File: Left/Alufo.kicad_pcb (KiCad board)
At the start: 2 copper layers, 139.7 x 88.9 mm, 67 parts, among them J1 USB_C_Receptacle_USB2.0_16P_2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, J3 USB_C_Receptacle_USB2.0_16P_2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, K11 PG1350, K12 PG1350, K13 PG1350, K14 PG1350, K15 PG1350, K16 PG1350, K21 PG1350, K22 PG1350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

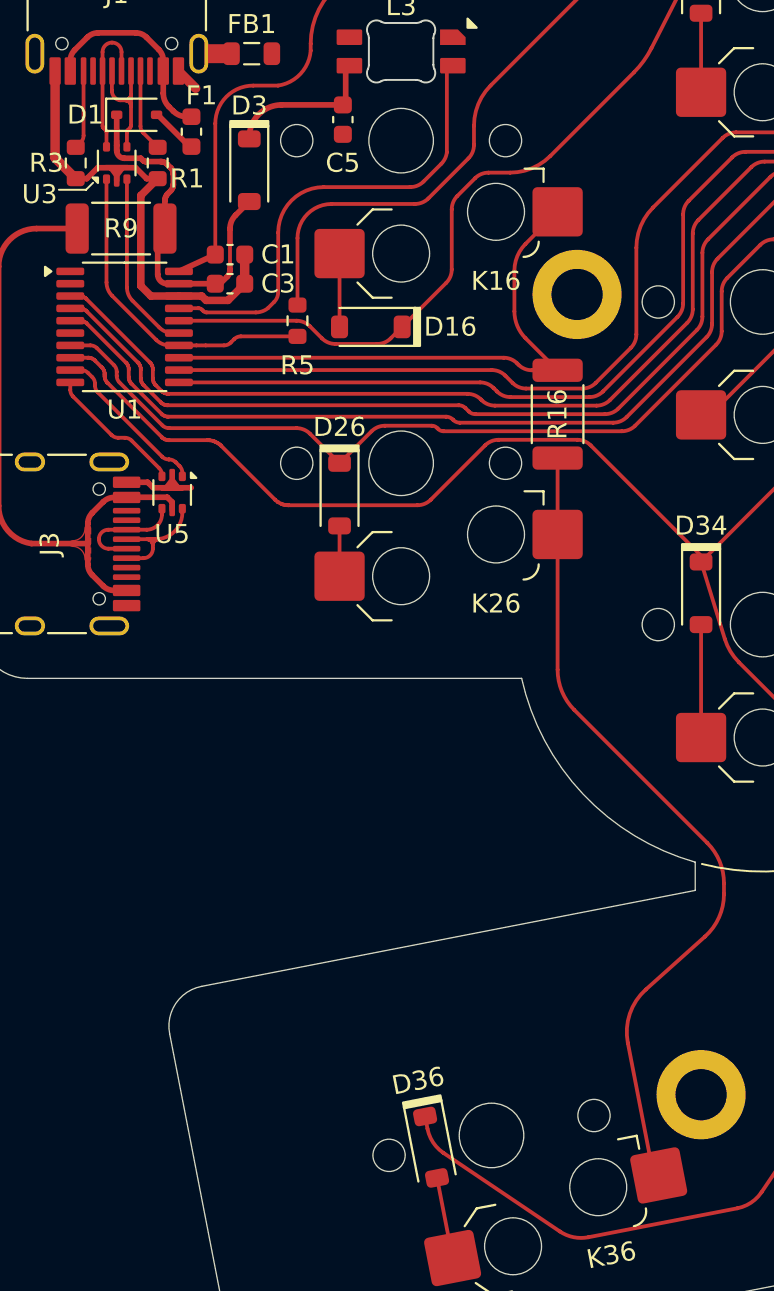
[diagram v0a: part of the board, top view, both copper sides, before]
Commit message: Power routing tweaks
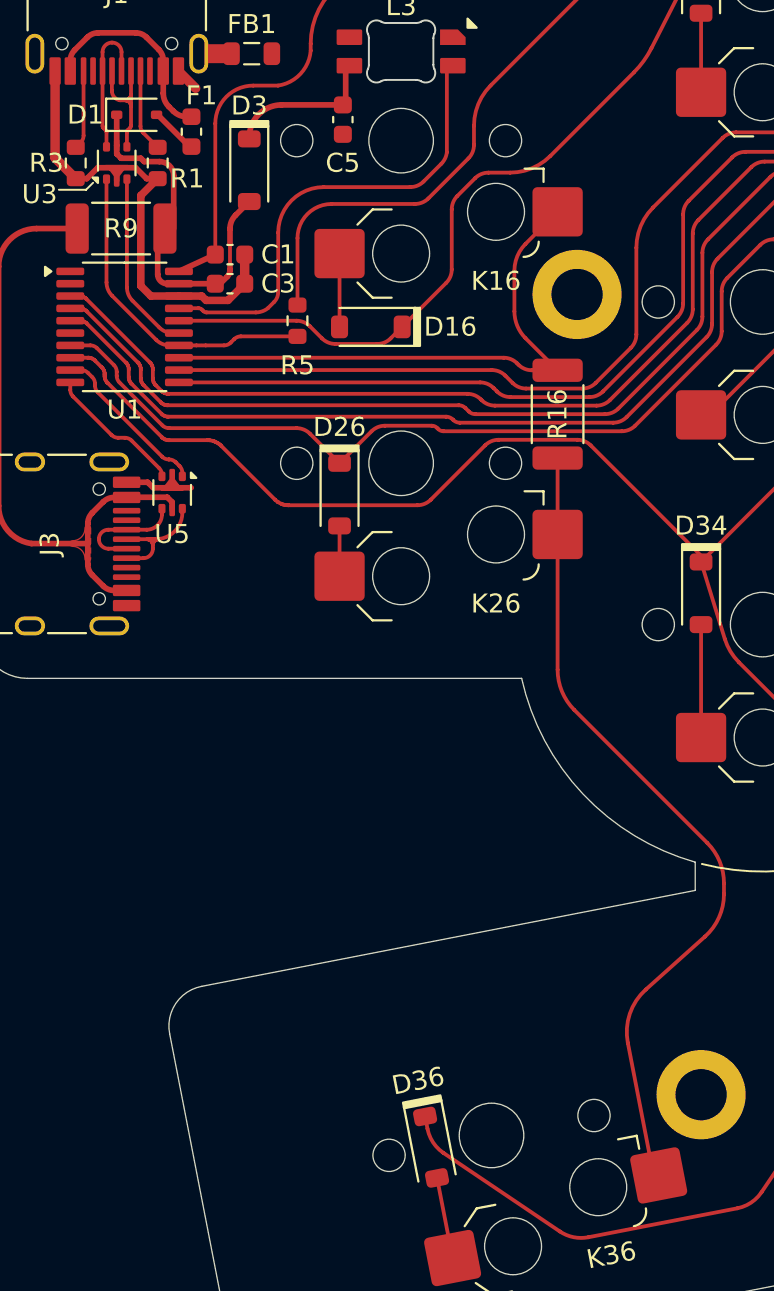
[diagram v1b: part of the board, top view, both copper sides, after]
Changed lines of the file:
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@@
 		(fp_arc
 			(start 1.749484 0.919719)
-			(mid 1.712511 0.81407)
+			(mid 1.712517 0.81407)
 			(end 1.699999 0.702842)
 			(stroke
@@
 		(fp_arc
 			(start 1.699999 -0.702843)
-			(mid 1.712528 -0.814069)
+			(mid 1.712527 -0.814069)
 			(end 1.749484 -0.919721)
 			(stroke
@@
 		(fp_arc
 			(start -1.749484 -0.919721)
-			(mid -1.638071 -1.504035)
+			(mid -1.638071 -1.504036)
 			(end -1.046711 -1.568299)
 			(stroke
@@
 		(net 47)
 	)
-	(segment
-		(start 118.038342 106.733149)
-		(end 118.34685 106.94124)
-		(width 0.2)
-		(layer "F.Cu")
-		(net 47)
-	)
 	(arc
 		(start 121.786884 92.118427)
@@
 	)
 	(segment
-		(start 91.277386 53.517356)
-		(end 91.316843 53.519)
-		(width 0.3)
-		(layer "F.Cu")
-		(net 61)
-	)
-	(segment
-		(start 92.737128 54.000498)
-		(end 92.771059 54.127177)
-		(width 0.3)
-		(layer "F.Cu")
-		(net 61)
-	)
-	(segment
-		(start 92.771059 54.127177)
-		(end 92.773 54.192749)
-		(width 0.3)
-		(layer "F.Cu")
-		(net 61)
-	)
-	(segment
-		(start 92.405061 53.620464)
-		(end 92.452805 53.665447)
-		(width 0.3)
-		(layer "F.Cu")
-		(net 61)
-	)
-	(segment
-		(start 92.164819 53.520976)
-		(end 92.291489 53.554905)
-		(width 0.3)
-		(layer "F.Cu")
-		(net 61)
-	)
-	(segment
 		(start 95.758 58.9915)
 		(end 95.758 57.8485)
@@
 	)
 	(segment
-		(start 92.099251 53.519)
-		(end 92.164819 53.520976)
-		(width 0.3)
-		(layer "F.Cu")
-		(net 61)
-	)
-	(segment
 		(start 89.789 51.054)
 		(end 89.789 52.669)
@@
 	)
 	(segment
-		(start 92.773 54.192749)
-		(end 92.773 54.713225)
-		(width 0.3)
-		(layer "F.Cu")
-		(net 61)
-	)
-	(segment
-		(start 92.291489 53.554905)
-		(end 92.405061 53.620464)
-		(width 0.3)
-		(layer "F.Cu")
-		(net 61)
-	)
-	(segment
 		(start 93.067 59.955)
 		(end 92.448 59.955)
@@
 	)
 	(segment
-		(start 92.626554 53.839196)
-		(end 92.671564 53.886918)
-		(width 0.3)
-		(layer "F.Cu")
-		(net 61)
-	)
-	(segment
-		(start 91.175422 53.460422)
-		(end 91.204473 53.487171)
-		(width 0.3)
-		(layer "F.Cu")
-		(net 61)
-	)
-	(segment
-		(start 92.331442 55.505367)
-		(end 92.3295 55.570939)
-		(width 0.3)
-		(layer "F.Cu")
-		(net 61)
-	)
-	(segment
-		(start 89.789 52.669)
-		(end 89.789 52.944001)
-		(width 0.3)
-		(layer "F.Cu")
-		(net 61)
-	)
-	(segment
-		(start 92.475946 55.217386)
-		(end 92.43094 55.265112)
-		(width 0.3)
-		(layer "F.Cu")
-		(net 61)
-	)
-	(segment
-		(start 91.059001 53.344001)
-		(end 91.175422 53.460422)
-		(width 0.3)
-		(layer "F.Cu")
-		(net 61)
-	)
-	(segment
-		(start 92.452805 53.665447)
-		(end 92.626554 53.839196)
+		(start 95.758 57.055214)
+		(end 95.758 57.8485)
 		(width 0.3)
 		(layer "F.Cu")
@@
 	)
 	(segment
-		(start 95.758 57.055214)
-		(end 95.758 57.8485)
+		(start 91.235976 53.520976)
+		(end 91.059001 53.344001)
 		(width 0.3)
 		(layer "F.Cu")
@@
 	)
 	(segment
-		(start 91.204473 53.487171)
-		(end 91.277386 53.517356)
-		(width 0.3)
-		(layer "F.Cu")
-		(net 61)
-	)
-	(segment
-		(start 92.736941 54.905394)
-		(end 92.671391 55.018921)
-		(width 0.3)
-		(layer "F.Cu")
-		(net 61)
-	)
-	(segment
-		(start 91.316843 53.519)
-		(end 92.099251 53.519)
+		(start 91.059001 53.344001)
+		(end 90.01979 53.344001)
 		(width 0.3)
 		(layer "F.Cu")
@@
 	)
 	(segment
-		(start 92.365376 55.37869)
-		(end 92.331442 55.505367)
-		(width 0.3)
-		(layer "F.Cu")
-		(net 61)
-	)
-	(segment
-		(start 92.43094 55.265112)
-		(end 92.365376 55.37869)
+		(start 90.01979 53.344001)
+		(end 89.789 53.113211)
 		(width 0.3)
 		(layer "F.Cu")
@@
 	)
 	(segment
-		(start 92.770876 54.778771)
-		(end 92.736941 54.905394)
-		(width 0.3)
-		(layer "F.Cu")
-		(net 61)
-	)
-	(segment
-		(start 92.3295 55.570939)
-		(end 92.3295 56.642)
+		(start 92.791999 57.0484)
+		(end 92.791999 54.270976)
 		(width 0.3)
 		(layer "F.Cu")
@@
 	)
 	(segment
-		(start 92.626553 55.066779)
-		(end 92.475946 55.217386)
+		(start 92.041999 53.520976)
+		(end 91.235976 53.520976)
 		(width 0.3)
 		(layer "F.Cu")
@@
 	)
 	(segment
-		(start 90.189 53.344001)
-		(end 91.059001 53.344001)
-		(width 0.3)
-		(layer "F.Cu")
-		(net 61)
-	)
-	(segment
-		(start 92.671391 55.018921)
-		(end 92.626553 55.066779)
-		(width 0.3)
-		(layer "F.Cu")
-		(net 61)
-	)
-	(segment
-		(start 92.773 54.713225)
-		(end 92.770876 54.778771)
-		(width 0.3)
-		(layer "F.Cu")
-		(net 61)
-	)
-	(segment
-		(start 92.671564 53.886918)
-		(end 92.737128 54.000498)
+		(start 89.789 53.113211)
+		(end 89.789 52.669)
 		(width 0.3)
 		(layer "F.Cu")
@@
 	)
 	(arc
-		(start 89.789 52.944001)
-		(mid 89.906157 53.226844)
-		(end 90.189 53.344001)
+		(start 95.758 59.228893)
+		(mid 95.71994 59.420234)
+		(end 95.611554 59.582446)
 		(width 0.3)
 		(layer "F.Cu")
@@
 	)
 	(arc
-		(start 95.758 59.228893)
-		(mid 95.71994 59.420234)
-		(end 95.611554 59.582446)
+		(start 92.791999 54.270976)
+		(mid 92.572329 53.740646)
+		(end 92.041999 53.520976)
 		(width 0.3)
 		(layer "F.Cu")
@@
 		(width 0.3)
 		(layer "F.Cu")
-		(net 62)
-	)
-	(segment
-		(start 93.479714 51.1555)
-		(end 93.726 51.1555)
-		(width 0.3)
-		(layer "F.Cu")

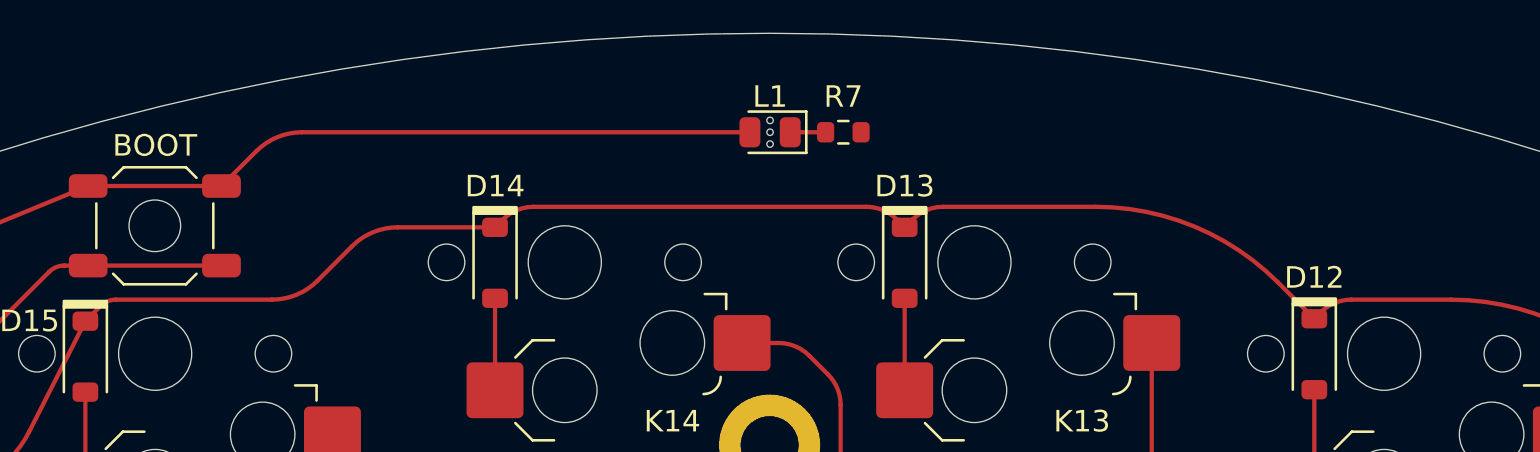
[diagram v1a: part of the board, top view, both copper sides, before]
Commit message: Fix boot access hole location
Because the lefthand side PCB will become the base for the righthand board (and vice versa), and because the boot button is no longer centred, the hole in the base to allow access to the button must be on the opposite side of the centreline to that button. This means the access hole needs to be a separate component and the boot switch footprint no longer needs a central hole.
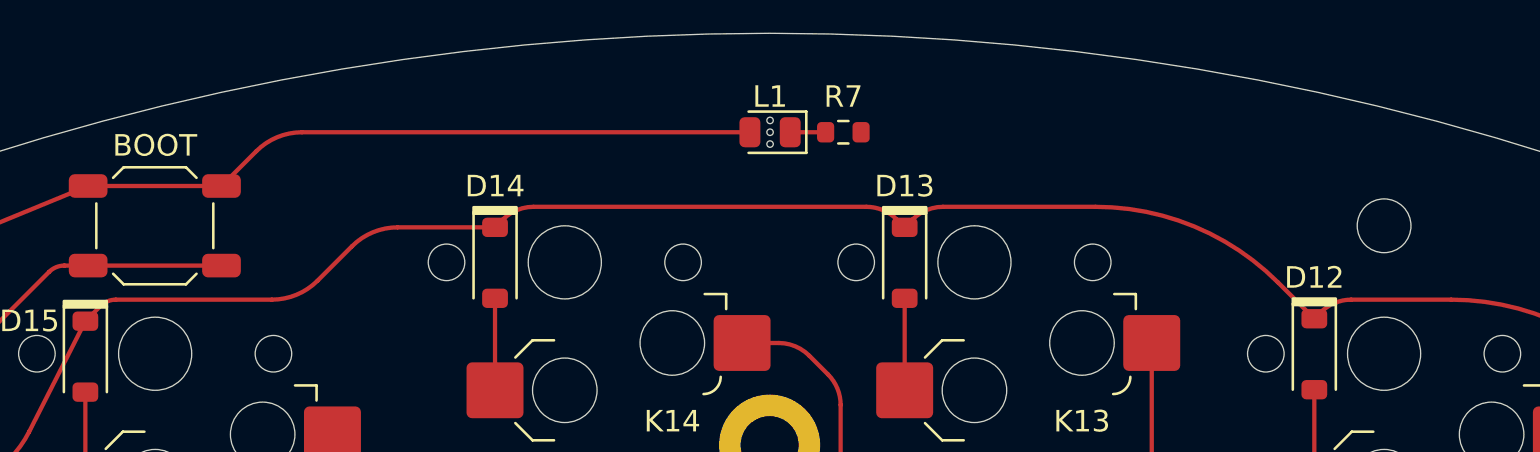
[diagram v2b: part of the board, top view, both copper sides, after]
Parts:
- added H6: BootAccess, MountingHole:MountingHole_2.5mm, F.Cu at (181.0, 38.0)
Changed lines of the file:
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@@
 		)
 	)
+	(footprint "MountingHole:MountingHole_2.5mm"
+		(layer "F.Cu")
+		(at 180.975001 37.966677)
+		(descr "Mounting Hole 2.5mm, no annular")
+		(tags "mounting hole 2.5mm no annular")
+		(property "Reference" "H6"
+			(at 0 -3.5 0)
+			(layer "F.SilkS")
+			(hide yes)
+			(effects
+				(font
+					(size 1 1)
+					(thickness 0.15)
+				)
+			)
+		)
+		(property "Value" "BootAccess"
+			(at 0 3.5 0)
+			(layer "F.Fab")
+			(hide yes)
+			(effects
+				(font
+					(size 1 1)
+					(thickness 0.15)
+				)
+			)
+		)
+		(property "Footprint" "MountingHole:MountingHole_2.5mm"
+			(at 0 0 0)
+			(unlocked yes)
+			(layer "F.Fab")
+			(hide yes)
+			(effects
+				(font
+					(size 1.27 1.27)
+					(thickness 0.15)
+				)
+			)
+		)
+		(property "Datasheet" ""
+			(at 0 0 0)
+			(unlocked yes)
+			(layer "F.Fab")
+			(hide yes)
+			(effects
+				(font
+					(size 1.27 1.27)
+					(thickness 0.15)
+				)
+			)
+		)
+		(property "Description" "Mounting Hole without connection"
+			(at 0 0 0)
+			(unlocked yes)
+			(layer "F.Fab")
+			(hide yes)
+			(effects
+				(font
+					(size 1.27 1.27)
+					(thickness 0.15)
+				)
+			)
+		)
+		(property ki_fp_filters "MountingHole*")
+		(sheetname "Root")
+		(sheetfile "Alufo.kicad_sch")
+		(attr exclude_from_pos_files exclude_from_bom)
+		(fp_circle
+			(center 0 0)
+			(end 2.5 0)
+			(stroke
+				(width 0.15)
+				(type solid)
+			)
+			(fill none)
+			(layer "Cmts.User")
+		)
+		(fp_circle
+			(center 0 0)
+			(end 2.75 0)
+			(stroke
+				(width 0.05)
+				(type solid)
+			)
+			(fill none)
+			(layer "F.CrtYd")
+		)
+		(fp_text user "${REFERENCE}"
+			(at 0 0 0)
+			(layer "F.Fab")
+			(effects
+				(font
+					(size 1 1)
+					(thickness 0.15)
+				)
+			)
+		)
+		(pad "" np_thru_hole circle
+			(at 0 0)
+			(size 2.5 2.5)
+			(drill 2.5)
+			(layers "*.Cu" "*.Mask")
+		)
+	)
 	(footprint "Project Library:MountingHole_2.2mm_M2_SMD_Solder_Nut"
 		(layer "F.Cu")
@@
 			(layer "User.6")
 		)
-		(fp_text user "KEEP-OUT ZONE"
-			(at -2.5 -0.2 0)
+		(fp_text user "No F.Cu tracks"
+			(at -2.5 0.2 0)
 			(layer "Cmts.User")
 			(effects
@@
 			)
 		)
-		(fp_text user "No F.Cu tracks"
-			(at 2.5 0.2 0)
+		(fp_text user "KEEP-OUT ZONE"
+			(at 2.5 -0.2 0)
 			(layer "Cmts.User")
 			(effects
@@
 		)
 		(fp_text user "No F.Cu tracks"
-			(at -2.5 0.2 0)
+			(at 2.5 0.2 0)
 			(layer "Cmts.User")
 			(effects
@@
 		)
 		(fp_text user "KEEP-OUT ZONE"
-			(at 2.5 -0.2 0)
+			(at -2.5 -0.2 0)
 			(layer "Cmts.User")
 			(effects
@@
 			)
 		)
-		(pad "" np_thru_hole circle
-			(at 0 0 180)
-			(size 2.4 2.4)
-			(drill 2.4)
-			(layers "F.Mask")
-		)
 		(pad "1" smd roundrect

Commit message: Update lefthand title block and dynamic text
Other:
- board text added: "${TITLE} v${REVISION} • ${COMPANY}"
- board text removed: "${PROJECTNAME} v${PCB_REVISION} • ${AUTHOR}"

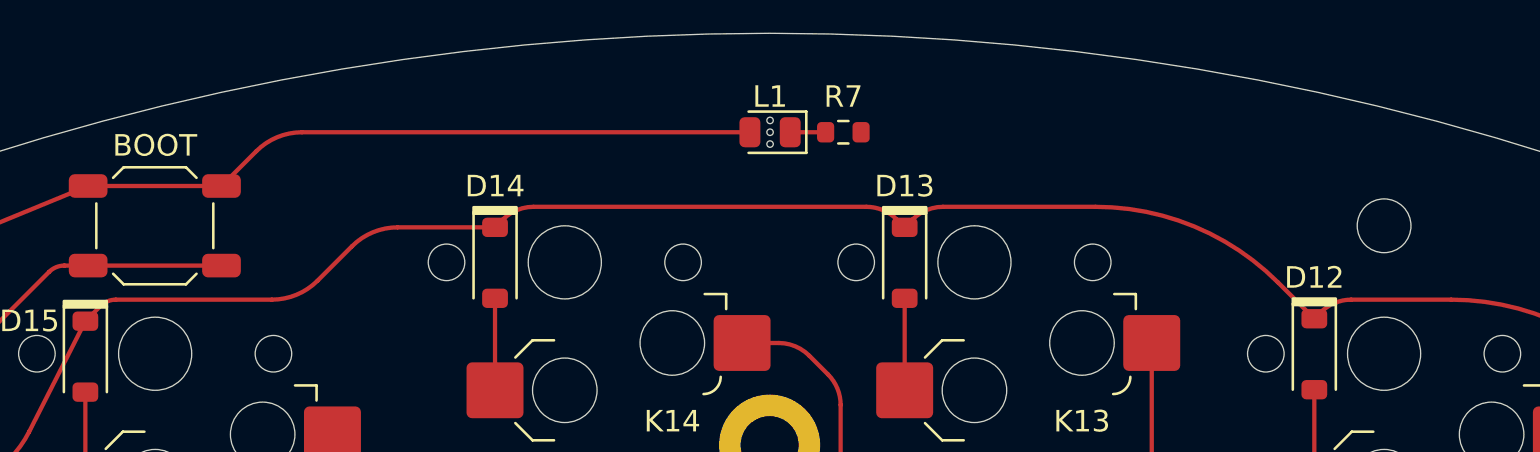
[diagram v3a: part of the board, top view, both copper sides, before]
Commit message: Revert boot access hole change
It was correct before!
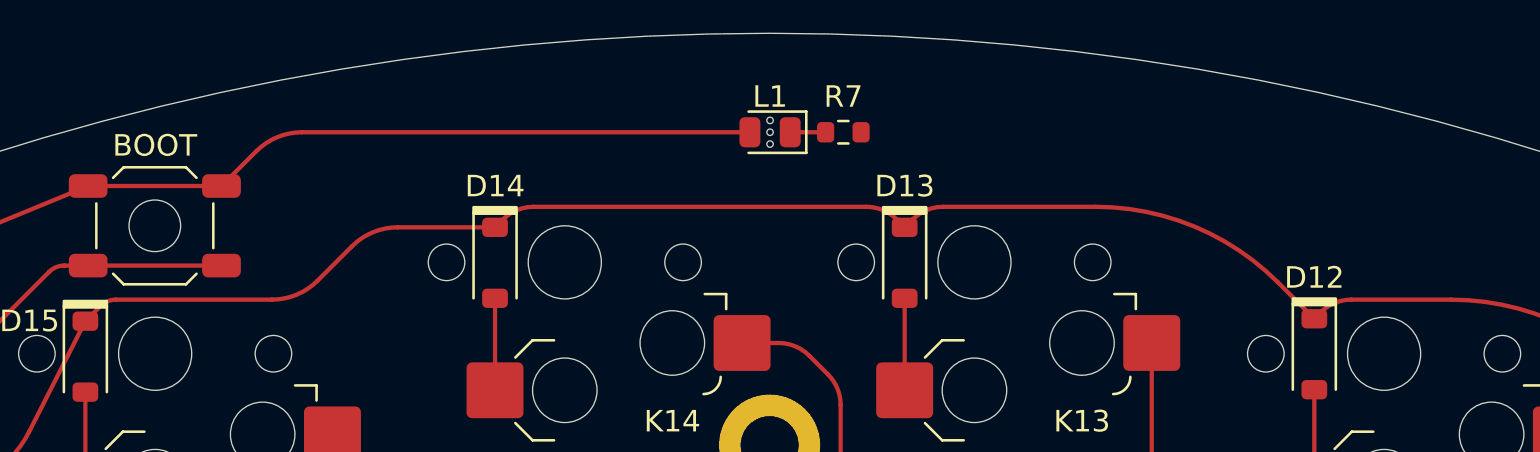
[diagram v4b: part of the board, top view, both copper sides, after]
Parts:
- removed H6: BootAccess, MountingHole:MountingHole_2.5mm
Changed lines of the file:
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@@
 		)
 	)
-	(footprint "MountingHole:MountingHole_2.5mm"
-		(layer "F.Cu")
-		(at 180.975001 37.966677)
-		(descr "Mounting Hole 2.5mm, no annular")
-		(tags "mounting hole 2.5mm no annular")
-		(property "Reference" "H6"
-			(at 0 -3.5 0)
-			(layer "F.SilkS")
-			(hide yes)
-			(effects
-				(font
-					(size 1 1)
-					(thickness 0.15)
-				)
-			)
-		)
-		(property "Value" "BootAccess"
-			(at 0 3.5 0)
-			(layer "F.Fab")
-			(hide yes)
-			(effects
-				(font
-					(size 1 1)
-					(thickness 0.15)
-				)
-			)
-		)
-		(property "Footprint" "MountingHole:MountingHole_2.5mm"
-			(at 0 0 0)
-			(unlocked yes)
-			(layer "F.Fab")
-			(hide yes)
-			(effects
-				(font
-					(size 1.27 1.27)
-					(thickness 0.15)
-				)
-			)
-		)
-		(property "Datasheet" ""
-			(at 0 0 0)
-			(unlocked yes)
-			(layer "F.Fab")
-			(hide yes)
-			(effects
-				(font
-					(size 1.27 1.27)
-					(thickness 0.15)
-				)
-			)
-		)
-		(property "Description" "Mounting Hole without connection"
-			(at 0 0 0)
-			(unlocked yes)
-			(layer "F.Fab")
-			(hide yes)
-			(effects
-				(font
-					(size 1.27 1.27)
-					(thickness 0.15)
-				)
-			)
-		)
-		(property ki_fp_filters "MountingHole*")
-		(sheetname "Root")
-		(sheetfile "Alufo.kicad_sch")
-		(attr exclude_from_pos_files exclude_from_bom)
-		(fp_circle
-			(center 0 0)
-			(end 2.5 0)
-			(stroke
-				(width 0.15)
-				(type solid)
-			)
-			(fill none)
-			(layer "Cmts.User")
-		)
-		(fp_circle
-			(center 0 0)
-			(end 2.75 0)
-			(stroke
-				(width 0.05)
-				(type solid)
-			)
-			(fill none)
-			(layer "F.CrtYd")
-		)
-		(fp_text user "${REFERENCE}"
-			(at 0 0 0)
-			(layer "F.Fab")
-			(effects
-				(font
-					(size 1 1)
-					(thickness 0.15)
-				)
-			)
-		)
-		(pad "" np_thru_hole circle
-			(at 0 0)
-			(size 2.5 2.5)
-			(drill 2.5)
-			(layers "*.Cu" "*.Mask")
-		)
-	)
 	(footprint "Project Library:MountingHole_2.2mm_M2_SMD_Solder_Nut"
 		(layer "F.Cu")
@@
 			)
 		)
+		(pad "" np_thru_hole circle
+			(at 0 0 180)
+			(size 2.4 2.4)
+			(drill 2.4)
+			(layers "F.Mask")
+		)
 		(pad "1" smd roundrect
